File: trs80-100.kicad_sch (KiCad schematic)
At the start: 114 parts, among them J1 Adapter Jack CN9, M27 4011, M28 4013, SW3 SLB-22BP-03, SW4 Reset Switch, SW5 SSP32201, T10 2SC2603, T11 2SC2603, T13 2SC2603(E), T14 2SC2603(E), T15 2SC2603(E), T16 2SC2603(E), T17 2SC2603(E), T18 2SC2603, T19 2SA1115, T20 2SC2603, T21 2SC2603(E), T22 2SC2603(E), T25 2SC2603, T27 2SC2603, T28 2SA1115, T9 2SC2603

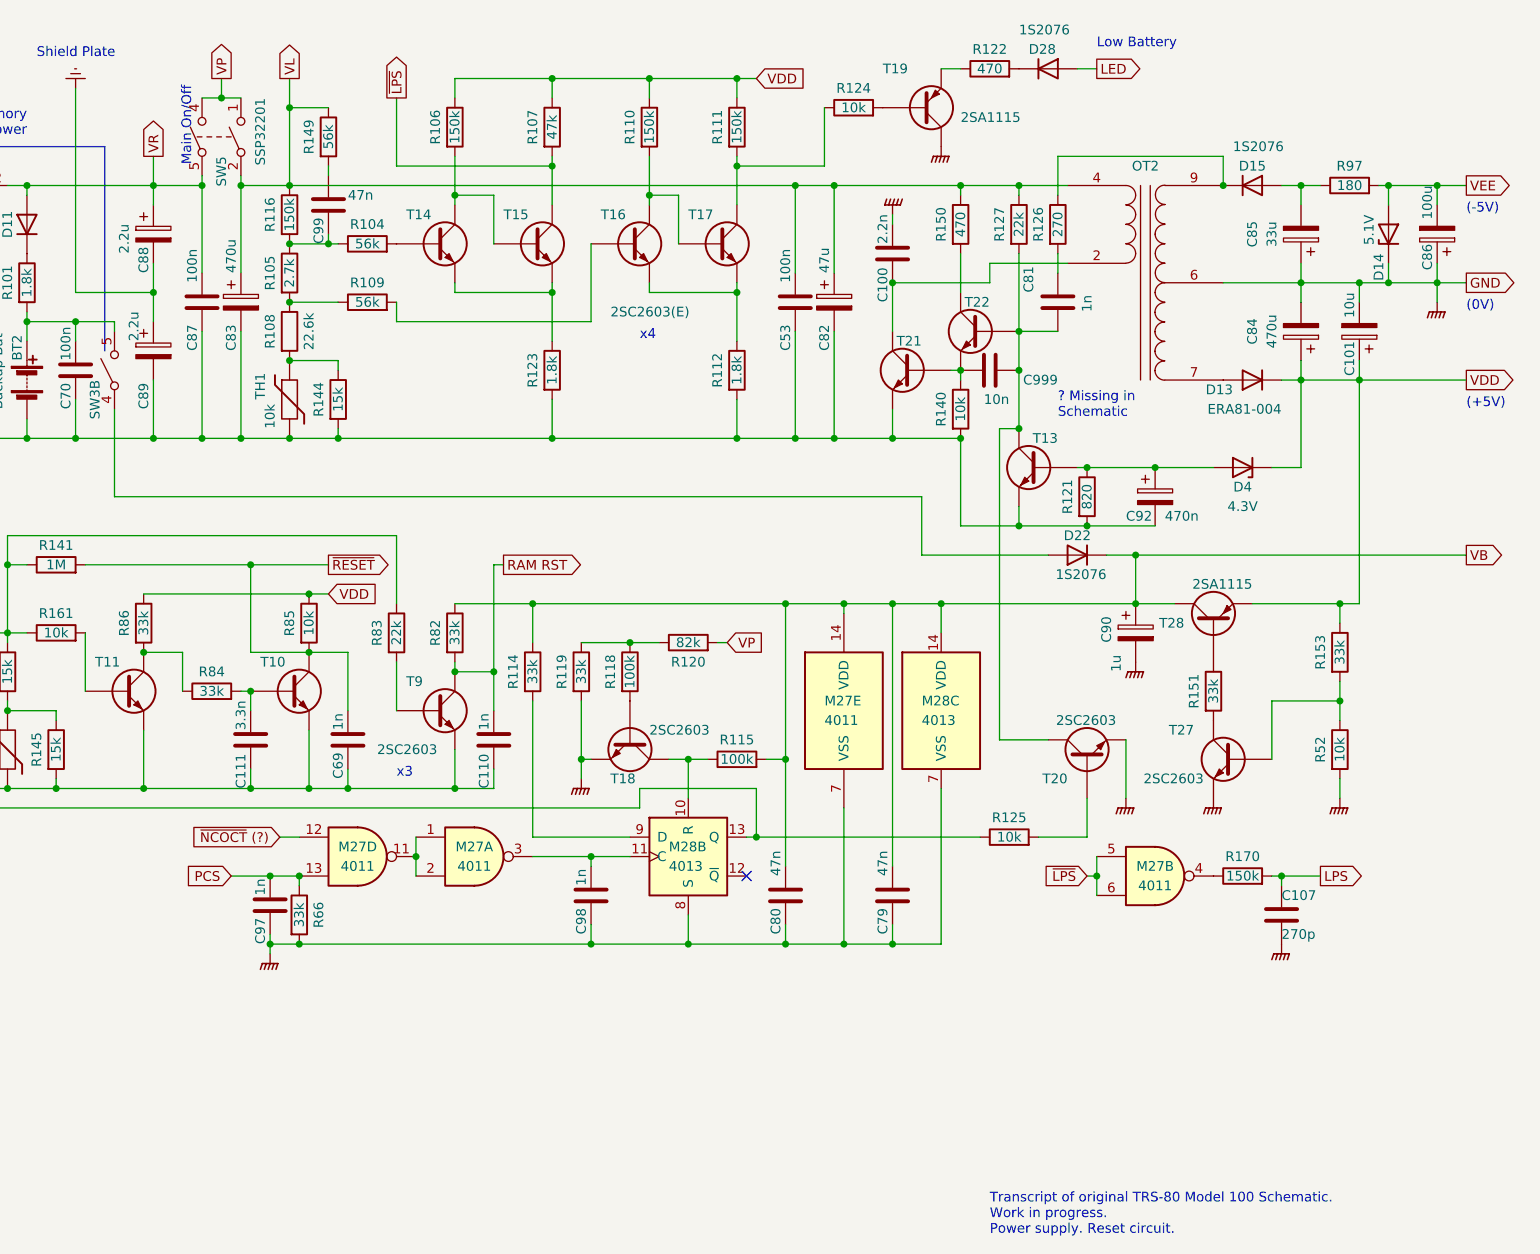
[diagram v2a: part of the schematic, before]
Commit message: Change paper size.
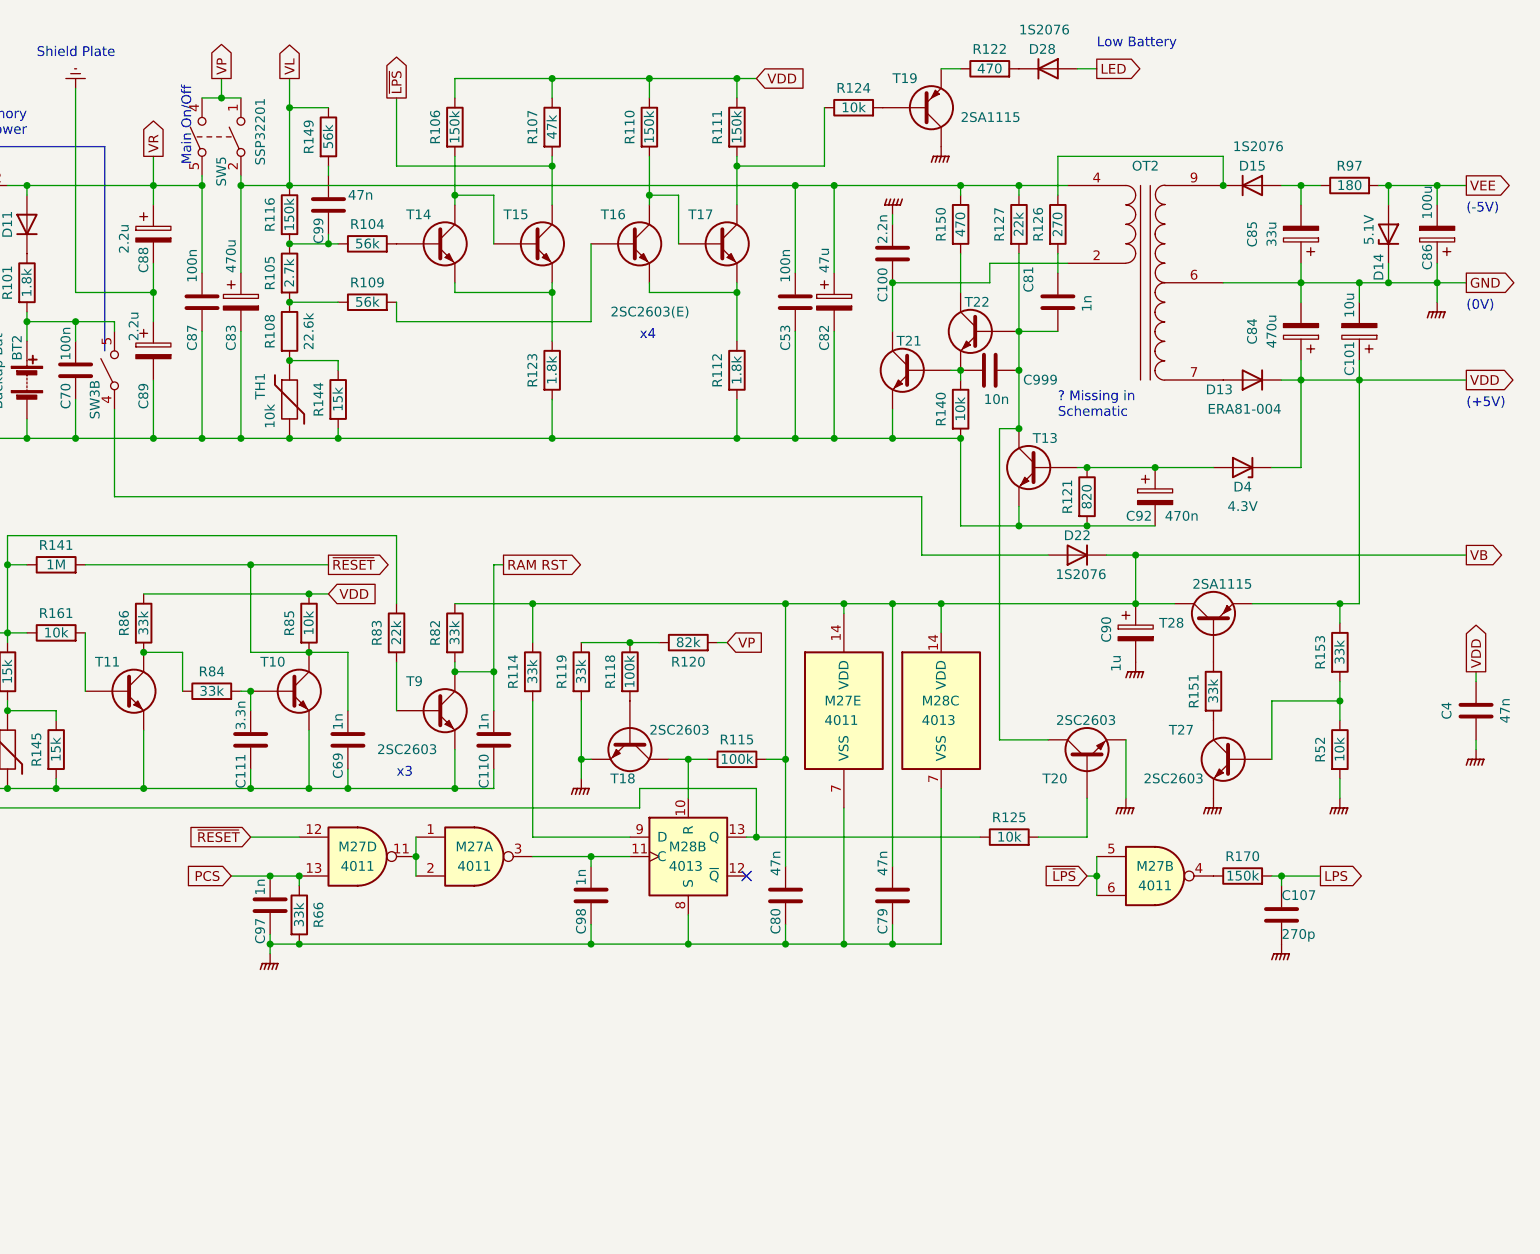
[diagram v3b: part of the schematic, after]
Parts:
- added C4: 47n, symbol Device:C
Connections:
- net ~{NCOCT} (?) is gone; now on net ~{RESET}: M27.12
- net GNDPWR: now also C4.2
- net VDD: now also C4.1
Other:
- note removed: "Transcript of original TRS-80 Model 100 Schematic. Work in progress. Power supply. Reset circuit."
- company: Transcribed by Henner Zeller -> Kyocera / Tandy
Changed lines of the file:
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@@
 (kicad_sch (version 20211123) (generator eeschema)
-  (paper "A4")
+  (paper "A3")
   (title_block
     (title "TRS-80 Model 100 Schematic")
     (date "1983")
-    (company "Transcribed by Henner Zeller")
+    (company "Kyocera / Tandy")
+    (comment 1 "https://github.com/hzeller/trs80-100-schematic (Henner Zeller)")
+    (comment 4 "Transcript of original TRS-80 Model 100 Schematic")
   )
   (junction (at 218.44 48.26) (diameter 0) (color 0 0 0 0)
@@
     (stroke (width 0) (type default) (color 0 0 0 0))
   )
+  (wire (pts (xy 241.3 107.95) (xy 241.3 109.22))
+    (stroke (width 0) (type default) (color 0 0 0 0))
+  )
   (wire (pts (xy 91.44 33.02) (xy 91.44 34.29))
     (stroke (width 0) (type default) (color 0 0 0 0))
@@
     (stroke (width 0) (type default) (color 0 0 0 0))
   )
+  (wire (pts (xy 241.3 99.06) (xy 241.3 100.33))
+    (stroke (width 0) (type default) (color 0 0 0 0))
+  )
   (wire (pts (xy 165.1 48.26) (xy 177.8 48.26))
     (stroke (width 0) (type default) (color 0 0 0 0))
@@
     (stroke (width 0) (type default) (color 0 0 0 0))
   )
-  (wire (pts (xy 85.09 120.65) (xy 87.63 120.65))
+  (wire (pts (xy 81.28 120.65) (xy 87.63 120.65))
     (stroke (width 0) (type default) (color 0 0 0 0))
   )
@@
     (effects (font (size 1.27 1.27)) (justify left bottom))
   )
-  (text "Transcript of original TRS-80 Model 100 Schematic.\nWork in progress.\nPower supply. Reset circuit."
-    (at 177.8 172.72 0)
-    (effects (font (size 1.27 1.27)) (justify left bottom))
-  )
   (text "x4" (at 132.08 55.88 0)
     (effects (font (size 1.27 1.27)) (justify left bottom))
@@
     )
   )
-  (global_label "~{NCOCT} (?)" (shape input) (at 85.09 120.65 180) (fields_autoplaced)
+  (global_label "~{RESET}" (shape input) (at 81.28 120.65 180) (fields_autoplaced)
     (effects (font (size 1.27 1.27)) (justify right))
-    (property "Intersheet References" "${INTERSHEET_REFS}" (id 0) (at 72.7588 120.5706 0)
+    (property "Intersheet References" "${INTERSHEET_REFS}" (id 0) (at 73.1217 120.5706 0)
       (effects (font (size 1.27 1.27)) (justify right) hide)
     )
@@
     )
   )
+  (global_label "VDD" (shape output) (at 241.3 99.06 90) (fields_autoplaced)
+    (effects (font (size 1.27 1.27)) (justify left))
+    (property "Intersheet References" "${INTERSHEET_REFS}" (id 0) (at 241.2206 93.0183 90)
+      (effects (font (size 1.27 1.27)) (justify left) hide)
+    )
+  )
   (symbol (lib_id "power:GNDPWR") (at 21.59 116.84 0) (unit 1)
     (in_bom yes) (on_board yes) (fields_autoplaced)
@@
     (pin "2")
   )
+  (symbol (lib_id "power:GNDPWR") (at 241.3 109.22 0) (unit 1)
+    (in_bom yes) (on_board yes) (fields_autoplaced)
+    (property "Reference" "#PWR?" (id 0) (at 241.3 114.3 0)
+      (effects (font (size 1.27 1.27)) hide)
+    )
+    (property "Value" "GNDPWR" (id 1) (at 241.173 114.3 0)
+      (effects (font (size 1.27 1.27)) hide)
+    )
+    (property "Footprint" "" (id 2) (at 241.3 110.49 0)
+      (effects (font (size 1.27 1.27)) hide)
+    )
+    (property "Datasheet" "" (id 3) (at 241.3 110.49 0)
+      (effects (font (size 1.27 1.27)) hide)
+    )
+    (pin "1")
+  )
   (symbol (lib_id "power:GNDPWR") (at 223.52 115.57 0) (unit 1)
     (in_bom yes) (on_board yes) (fields_autoplaced)
@@
   (symbol (lib_id "Transistor_BJT:2N3906") (at 168.91 25.4 0) (mirror x) (unit 1)
     (in_bom yes) (on_board yes)
-    (property "Reference" "T19" (id 0) (at 163.83 20.32 0)
+    (property "Reference" "T19" (id 0) (at 165.1 21.59 0)
       (effects (font (size 1.27 1.27)) (justify left))
     )
@@
     (pin "3")
   )
+  (symbol (lib_id "Device:C") (at 241.3 104.14 0) (unit 1)
+    (in_bom yes) (on_board yes)
+    (property "Reference" "C4" (id 0) (at 237.49 104.14 90))
+    (property "Value" "47n" (id 1) (at 245.11 104.14 90))
+    (property "Footprint" "" (id 2) (at 242.2652 107.95 0)
+      (effects (font (size 1.27 1.27)) hide)
+    )
+    (property "Datasheet" "~" (id 3) (at 241.3 104.14 0)
+      (effects (font (size 1.27 1.27)) hide)
+    )
+    (pin "1")
+    (pin "2")
+  )
   (symbol (lib_id "Device:C") (at 125.73 128.27 0) (unit 1)
     (in_bom yes) (on_board yes)
@@
       (reference "#PWR?") (unit 1) (value "GNDPWR") (footprint "")
     )
+    (path "/31ff9f1b-d298-4ced-9e92-c1f8afb17589"
+      (reference "#PWR?") (unit 1) (value "GNDPWR") (footprint "")
+    )
     (path "/32004c85-6aba-40ea-ad59-83e820c4ad5b"
       (reference "#PWR?") (unit 1) (value "GNDPWR") (footprint "")
@@
       (reference "BT2") (unit 1) (value "Backup Bat") (footprint "")
     )
+    (path "/d3e65640-0ba6-41da-ba7f-e2d7f224744e"
+      (reference "C4") (unit 1) (value "47n") (footprint "")
+    )
     (path "/f06b55f0-277e-45e6-beca-83acd930e45d"

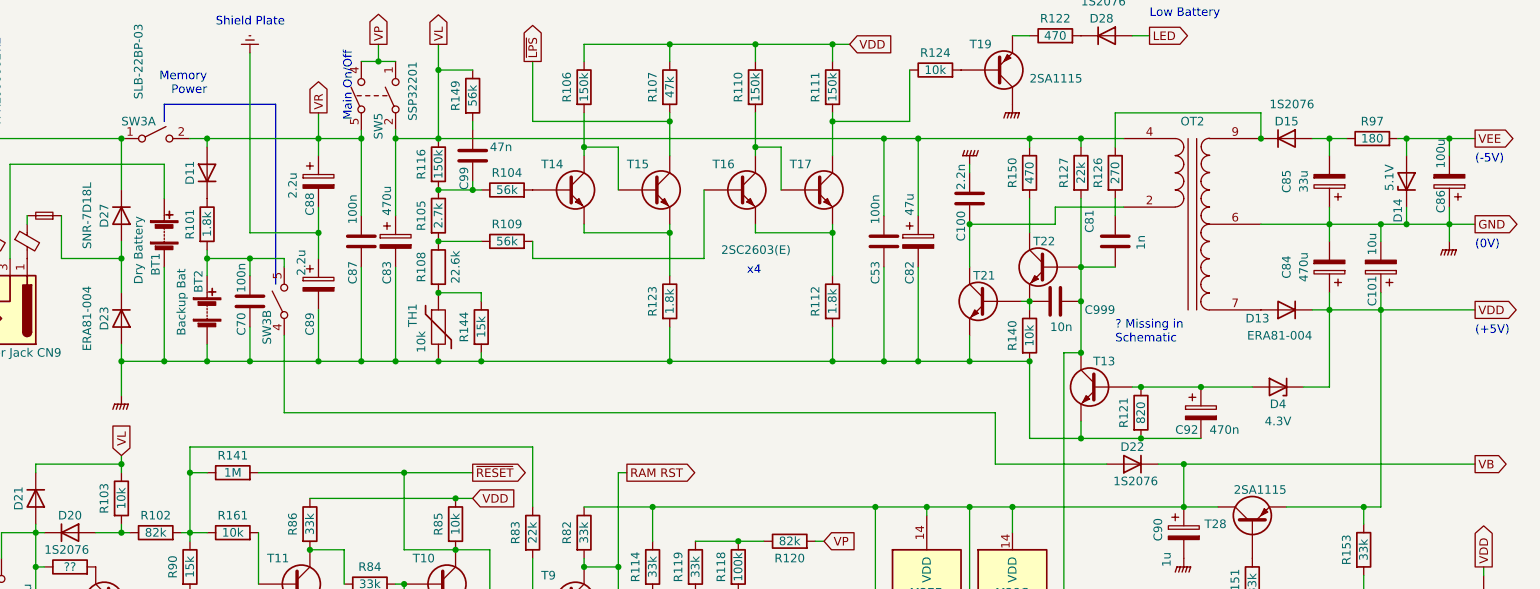
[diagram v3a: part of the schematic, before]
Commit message: Start local symbol library and copy locally modified symbols into it.
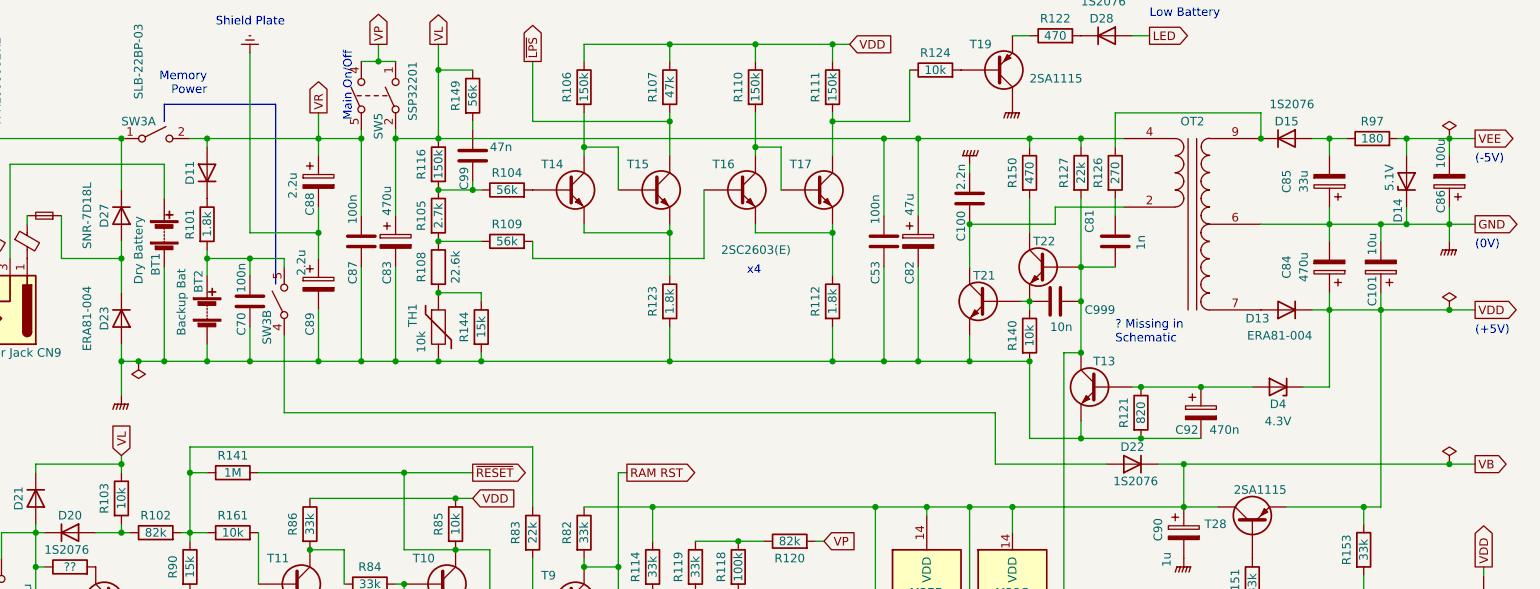
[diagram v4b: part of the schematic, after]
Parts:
- M28: symbol 4xxx:4013 -> trs80-100:4013-reset-up
- OT2: symbol Device:Transformer_1P_SS -> trs80-100:TN22A
- SW3: symbol Switch:SW_DPST_x2 -> trs80-100:SLB-22BP-03
- SW5: symbol Switch:SW_DPST -> trs80-100:SSP32201
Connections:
- net GNDREF: no longer names the net of C88.2, C89.1

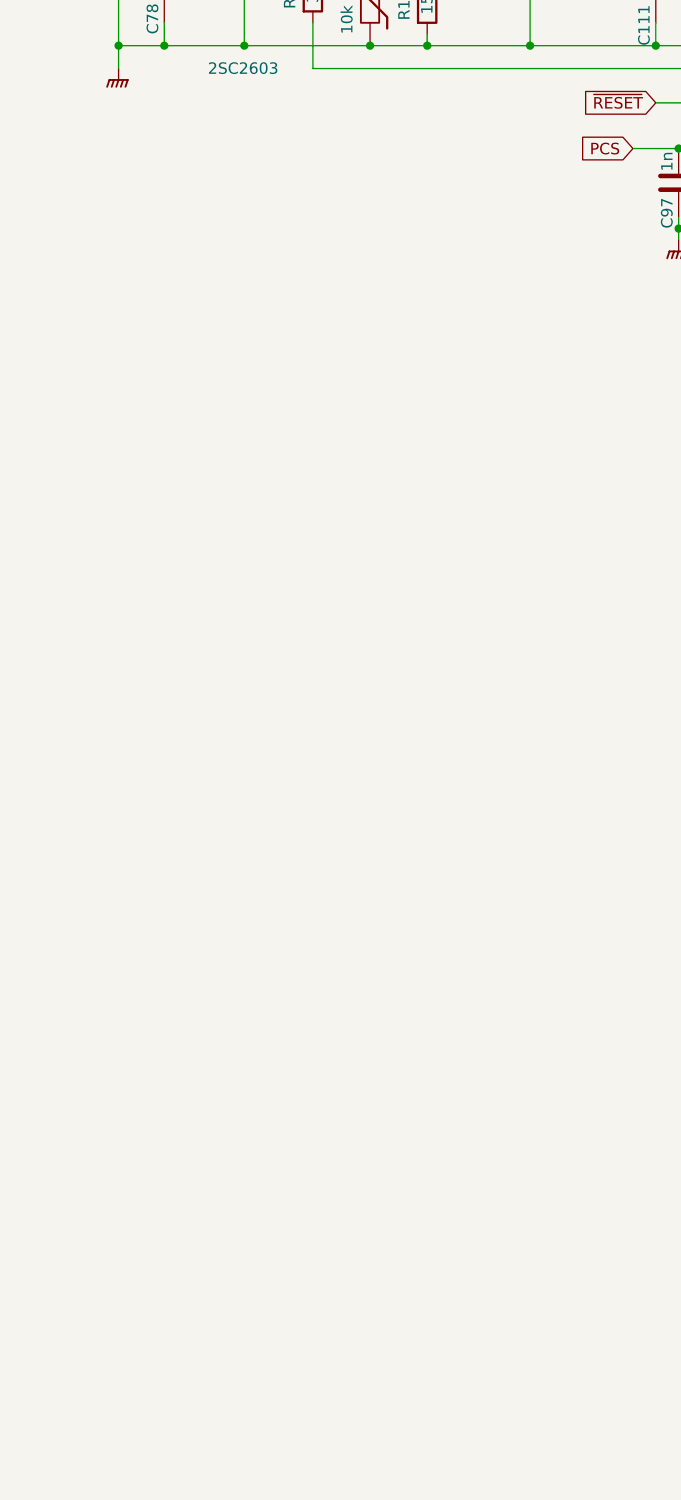
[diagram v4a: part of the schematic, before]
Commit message: Add connector symbols.
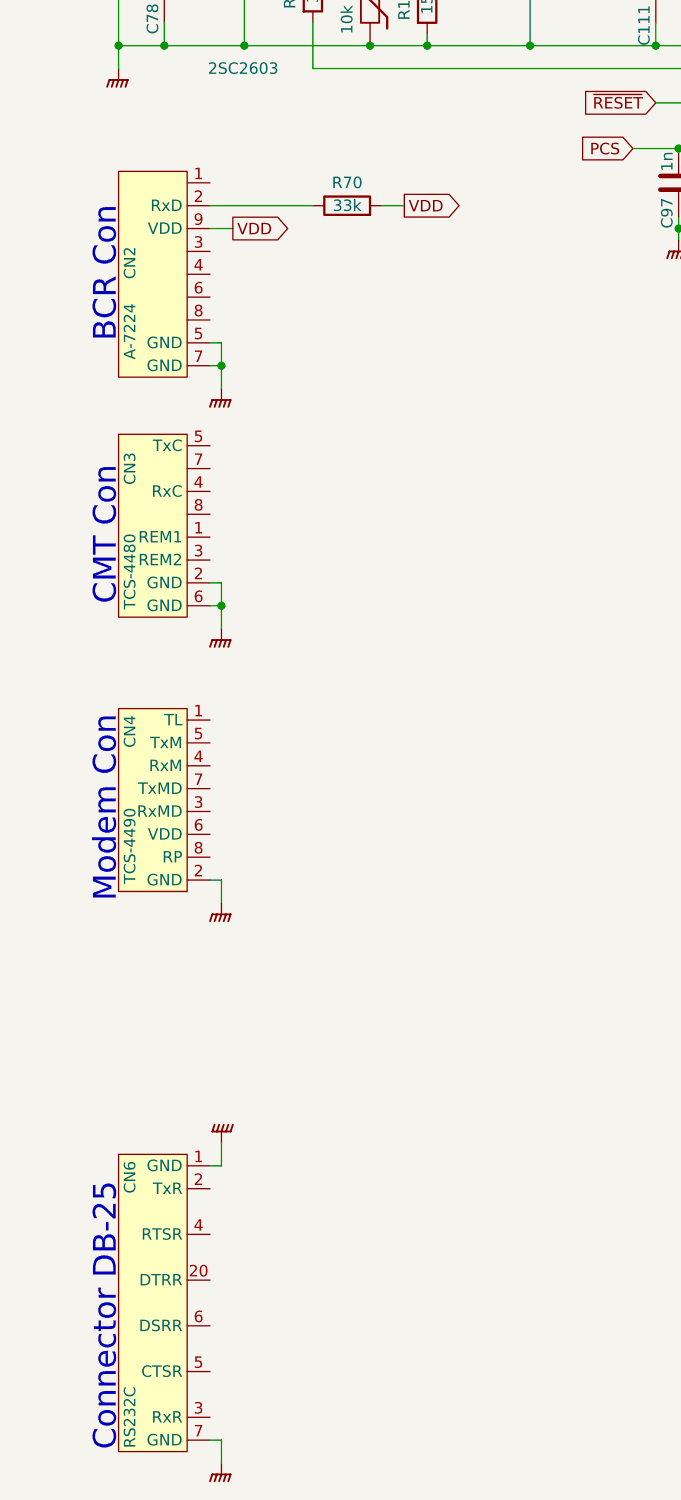
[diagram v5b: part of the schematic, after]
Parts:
- added CN2: A-7224, symbol trs80-100:A-7224
- added CN3: TCS-4480, symbol trs80-100:TCS-4480
- added CN4: TCS-4490, symbol trs80-100:TCS-4490
- added CN6: RS232C, symbol trs80-100:RS232C
- added R70: 33k, symbol Device:R
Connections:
- net GNDPWR: now also CN2.5 (GND), CN2.7 (GND), CN3.2 (GND), CN3.6 (GND), CN4.2 (GND), CN6.1 (GND), CN6.7 (GND)
- net VDD: now also CN2.9 (VDD), R70.2
- new net: CN2.2 (RxD), R70.1
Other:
- note added: "BCR Con"
- note added: "CMT Con"
- note added: "Connector DB-25"
- note added: "Modem Con"
